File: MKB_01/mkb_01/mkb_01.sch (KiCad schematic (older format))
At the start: 360 parts, among them J1 USB_C_Receptacle_USB2.0, J2 SW_Push, K1 SW_Push, M1 SW_Push, P1 SW_Push, Q1 SW_Push, Q2 BSP318, Q3 BSP318, T1 SW_Push, U1 LD1117S33TR_SOT223, U2 STM32F070CBTx, U3 SW_Push, X1 SW_Push, Y1 SW_Push, Y2 Crystal

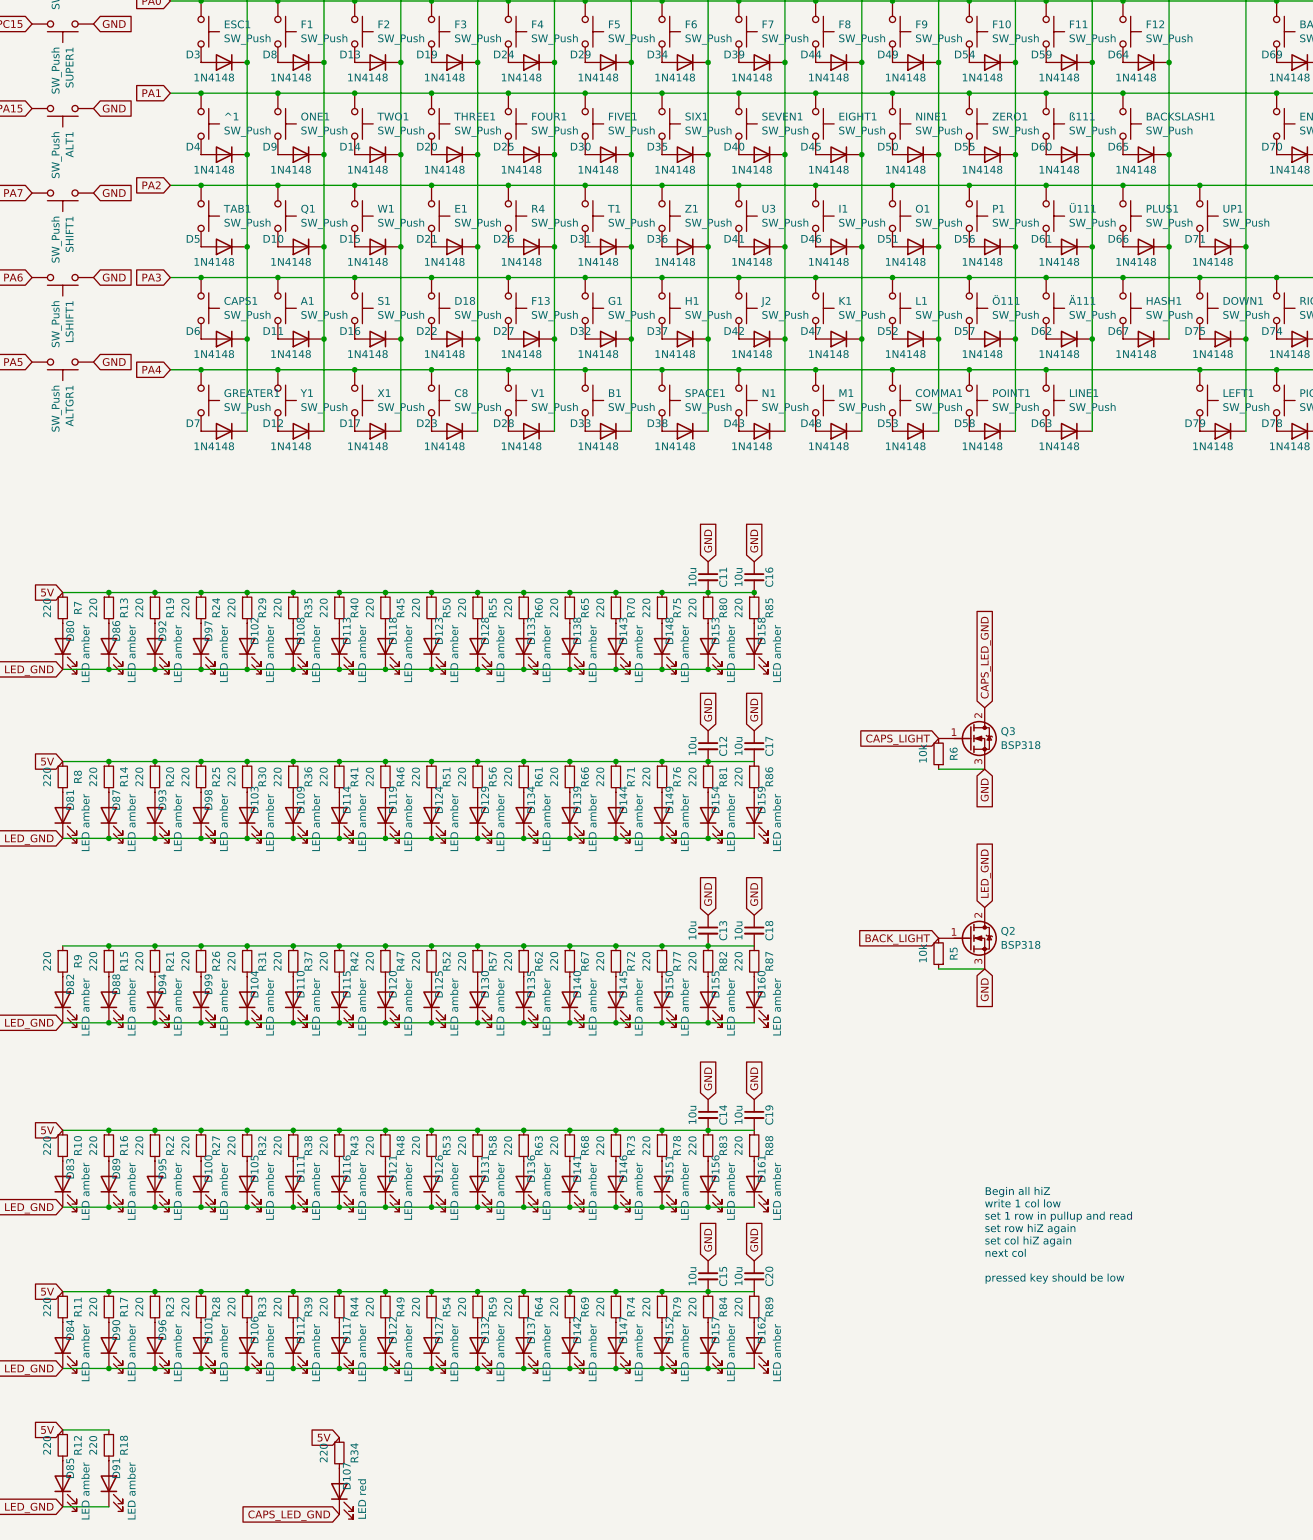
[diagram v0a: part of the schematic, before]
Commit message: added FN key fixed layout
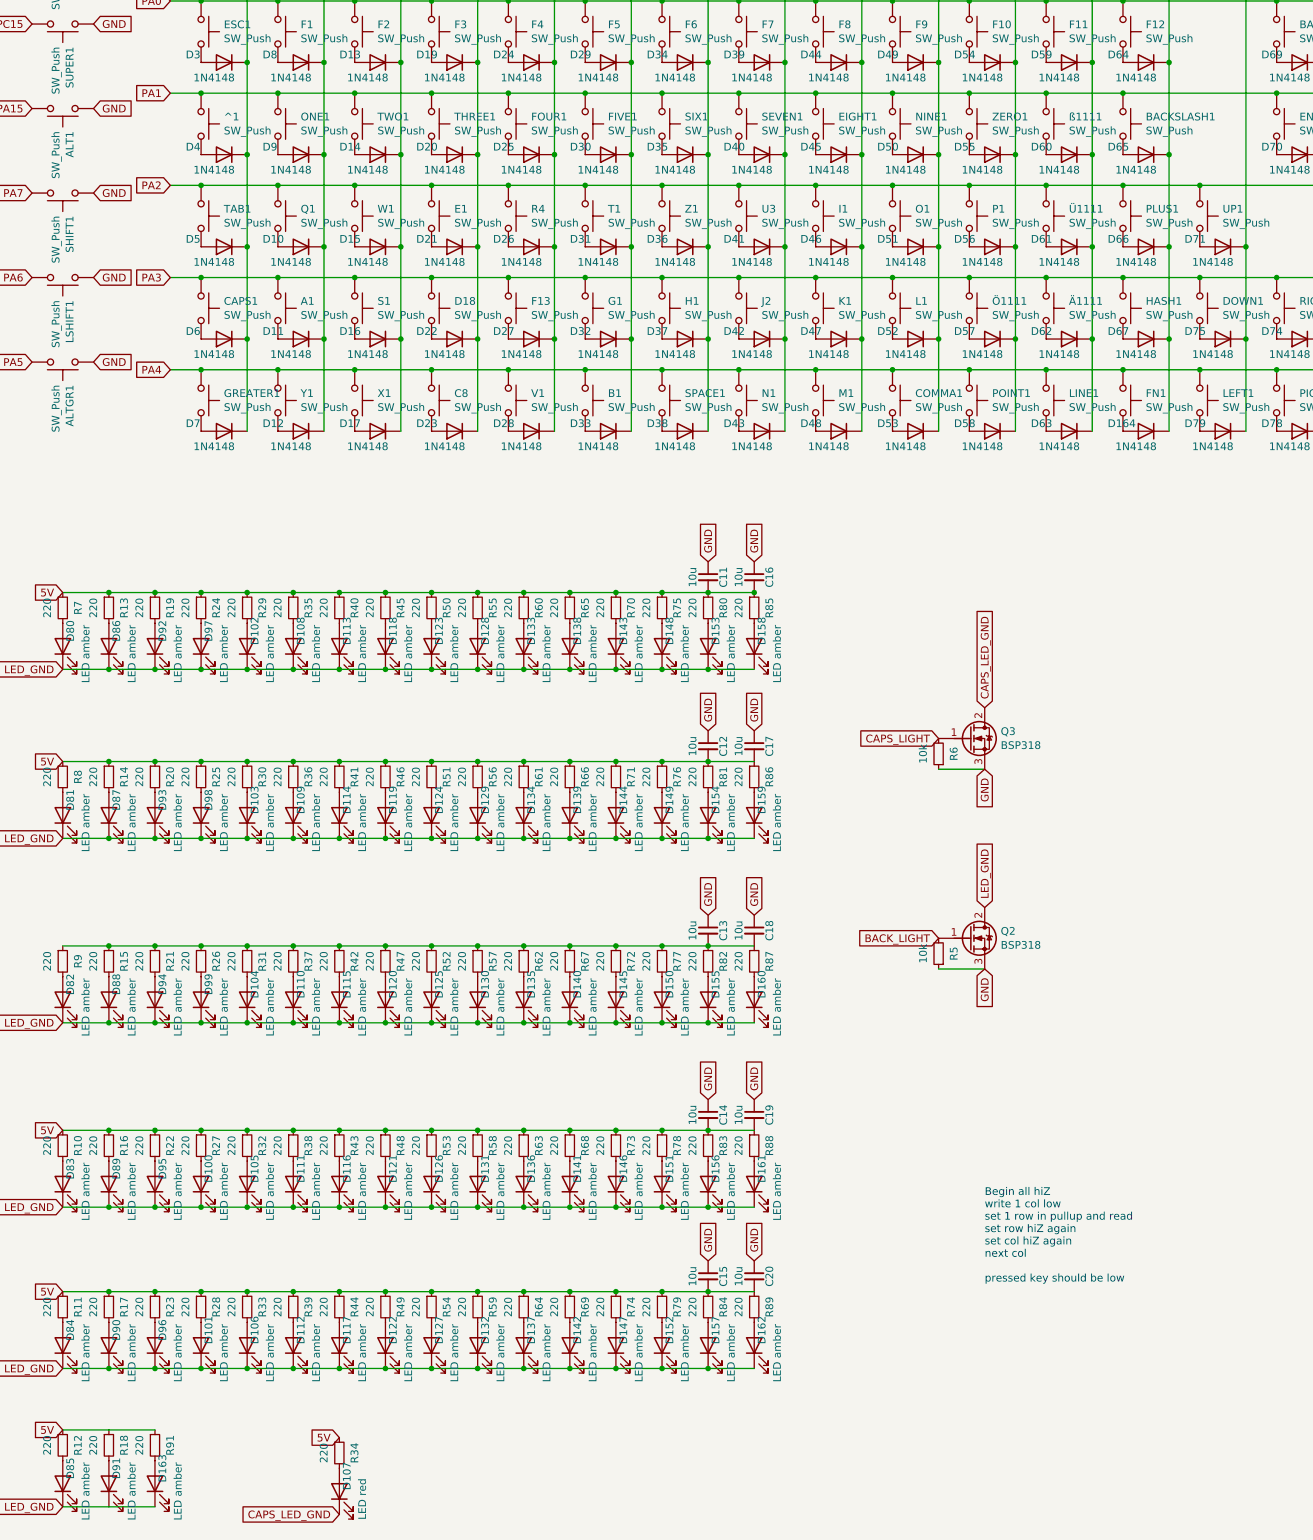
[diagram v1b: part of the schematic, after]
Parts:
- added D163: LED amber, LED_SMD:LED_0402_1005Metric_Pad0.77x0.64mm_HandSolder, symbol Device:LED
- added D164: 1N4148, Diode_SMD:D_0603_1608Metric_Pad1.05x0.95mm_HandSolder, symbol Diode:1N4148
- added FN1: SW_Push, Button_Switch_Keyboard:SW_Cherry_MX_1.00u_PCB, symbol Switch:SW_Push
- added R91: 220, Resistor_SMD:R_0603_1608Metric_Pad0.98x0.95mm_HandSolder, symbol Device:R_Small
- LSHIFT1, PICDOWN1, SUPER1: footprint Button_Switch_Keyboard:SW_Cherry_MX_1.25u_PCB -> Button_Switch_Keyboard:SW_Cherry_MX_1.00u_PCB
- SHIFT1: footprint Button_Switch_Keyboard:SW_Cherry_MX_1.25u_PCB -> Button_Switch_Keyboard:SW_Cherry_MX_2.00u_PCB
- renumbered Ä111 to Ä1111, Ö111 to Ö1111, Ü111 to Ü1111, ß111 to ß1111
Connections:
- net 5V: now also R91.1
- net LED_GND: now also D163.1 (K)
- net PA4: now also FN1.1
- net PB12: now also D164.1 (K)
- new net: D164.2 (A), FN1.2
- new net: D163.2 (A), R91.2
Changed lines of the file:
@@
 $EndComp
 $Comp
-L Switch:SW_Push ß111
+L Switch:SW_Push ß1111
 U 1 1 604A27F2
 P 13250 2000
-F 0 "ß111" V 13204 2148 50  0000 L CNN
+F 0 "ß1111" V 13204 2148 50  0000 L CNN
 F 1 "SW_Push" V 13295 2148 50  0000 L CNN
 F 2 "Button_Switch_Keyboard:SW_Cherry_MX_1.00u_PCB" H 13250 2200 50  0001 C CNN
@@
 $EndComp
 $Comp
-L Switch:SW_Push Ü111
+L Switch:SW_Push Ü1111
 U 1 1 604B7861
 P 13250 2600
-F 0 "Ü111" V 13204 2748 50  0000 L CNN
+F 0 "Ü1111" V 13204 2748 50  0000 L CNN
 F 1 "SW_Push" V 13295 2748 50  0000 L CNN
 F 2 "Button_Switch_Keyboard:SW_Cherry_MX_1.00u_PCB" H 13250 2800 50  0001 C CNN
@@
 F 0 "PICDOWN1" V 14704 3948 50  0000 L CNN
 F 1 "SW_Push" V 14795 3948 50  0000 L CNN
-F 2 "Button_Switch_Keyboard:SW_Cherry_MX_1.25u_PCB" H 14750 4000 50  0001 C CNN
+F 2 "Button_Switch_Keyboard:SW_Cherry_MX_1.00u_PCB" H 14750 4000 50  0001 C CNN
 F 3 "~" H 14750 4000 50  0001 C CNN
 	1    14750 3800
@@
 $EndComp
 $Comp
-L Switch:SW_Push Ö111
+L Switch:SW_Push Ö1111
 U 1 1 604C336A
 P 12750 3200
-F 0 "Ö111" V 12704 3348 50  0000 L CNN
+F 0 "Ö1111" V 12704 3348 50  0000 L CNN
 F 1 "SW_Push" V 12795 3348 50  0000 L CNN
 F 2 "Button_Switch_Keyboard:SW_Cherry_MX_1.00u_PCB" H 12750 3400 50  0001 C CNN
@@
 $EndComp
 $Comp
-L Switch:SW_Push Ä111
+L Switch:SW_Push Ä1111
 U 1 1 604C3376
 P 13250 3200
-F 0 "Ä111" V 13204 3348 50  0000 L CNN
+F 0 "Ä1111" V 13204 3348 50  0000 L CNN
 F 1 "SW_Push" V 13295 3348 50  0000 L CNN
 F 2 "Button_Switch_Keyboard:SW_Cherry_MX_1.00u_PCB" H 13250 3400 50  0001 C CNN
@@
 F 0 "SUPER1" V 6804 1498 50  0000 L CNN
 F 1 "SW_Push" V 6895 1498 50  0000 L CNN
-F 2 "Button_Switch_Keyboard:SW_Cherry_MX_1.25u_PCB" H 6850 1550 50  0001 C CNN
+F 2 "Button_Switch_Keyboard:SW_Cherry_MX_1.00u_PCB" H 6850 1550 50  0001 C CNN
 F 3 "~" H 6850 1550 50  0001 C CNN
 	1    6850 1350
@@
 F 0 "SHIFT1" V 6804 2598 50  0000 L CNN
 F 1 "SW_Push" V 6895 2598 50  0000 L CNN
-F 2 "Button_Switch_Keyboard:SW_Cherry_MX_1.25u_PCB" H 6850 2650 50  0001 C CNN
+F 2 "Button_Switch_Keyboard:SW_Cherry_MX_2.00u_PCB" H 6850 2650 50  0001 C CNN
 F 3 "~" H 6850 2650 50  0001 C CNN
 	1    6850 2450
@@
 F 0 "LSHIFT1" V 6804 3148 50  0000 L CNN
 F 1 "SW_Push" V 6895 3148 50  0000 L CNN
-F 2 "Button_Switch_Keyboard:SW_Cherry_MX_1.25u_PCB" H 6850 3200 50  0001 C CNN
+F 2 "Button_Switch_Keyboard:SW_Cherry_MX_1.00u_PCB" H 6850 3200 50  0001 C CNN
 F 3 "~" H 6850 3200 50  0001 C CNN
 	1    6850 3000
@@
 	14550 1100 14550 2800
 Wire Wire Line
-	13250 3600 14250 3600
+	13250 3600 13750 3600
 Connection ~ 13250 3600
 Connection ~ 14250 3600
@@
 	15550 3400 15550 4000
 Connection ~ 15550 3400
+$Comp
+L Switch:SW_Push FN1
+U 1 1 604CEAFC
+P 13750 3800
+F 0 "FN1" V 13704 3948 50  0000 L CNN
+F 1 "SW_Push" V 13795 3948 50  0000 L CNN
+F 2 "Button_Switch_Keyboard:SW_Cherry_MX_1.00u_PCB" H 13750 4000 50  0001 C CNN
+F 3 "~" H 13750 4000 50  0001 C CNN
+	1    13750 3800
+	0    1    1    0
+$EndComp
+$Comp
+L Diode:1N4148 D164
+U 1 1 604CEB02
+P 13900 4000
+F 0 "D164" H 14150 3950 50  0000 R CNN
+F 1 "1N4148" H 14100 4100 50  0000 R CNN
+F 2 "Diode_SMD:D_0603_1608Metric_Pad1.05x0.95mm_HandSolder" H 13900 3825 50  0001 C CNN
+F 3 "https://assets.nexperia.com/documents/data-sheet/1N4148_1N4448.pdf" H 13900 4000 50  0001 C CNN
+	1    13900 4000
+	-1   0    0    1
+$EndComp
+Connection ~ 13750 3600
+Wire Wire Line
+	13750 3600 14250 3600
+Wire Wire Line
+	14050 3400 14050 4000
+Connection ~ 14050 3400
+$Comp
+L Device:LED D163
+U 1 1 6056B7A9
+P 7450 10850
+F 0 "D163" H 7550 10800 50  0000 C CNN
+F 1 "LED amber" H 7400 10700 50  0000 C CNN
+F 2 "LED_SMD:LED_0402_1005Metric_Pad0.77x0.64mm_HandSolder" H 7450 10850 50  0001 C CNN
+F 3 "https://www.farnell.com/datasheets/2344828.pdf" H 7450 10850 50  0001 C CNN
+F 4 "https://de.farnell.com/broadcom-limited/hsma-c280/led-gelb-90mcd-592nm-0402/dp/2494320RL" H 7450 10850 50  0001 C CNN "URL"
+	1    7450 10850
+	0    -1   -1   0
+$EndComp
+$Comp
+L Device:R_Small R91
+U 1 1 6056B7B0
+P 7450 10600
+F 0 "R91" V 7550 10600 50  0000 C CNN
+F 1 "220" V 7350 10600 50  0000 C CNN
+F 2 "Resistor_SMD:R_0603_1608Metric_Pad0.98x0.95mm_HandSolder" H 7450 10600 50  0001 C CNN
+F 3 "~" H 7450 10600 50  0001 C CNN
+F 4 "https://de.farnell.com/walsin/wr06x221-jtl/dickschichtwiderstand-220r-5-0/dp/2670694" V 7450 10600 50  0001 C CNN "URL"
+	1    7450 10600
+	1    0    0    -1
+$EndComp
+Wire Wire Line
+	7150 10500 7450 10500
+Wire Wire Line
+	7150 11000 7450 11000
 $EndSCHEMATC

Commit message: changed quartz, finished placing and layers, some routing done
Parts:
- added H2, H3, H4, H5, H6, H7, H8, H9: MountingHole, MountingHole:MountingHole_3.2mm_M3_DIN965_Pad_TopBottom, symbol Mechanical:MountingHole
- Y2: footprint Crystal:Crystal_SMD_SeikoEpson_MA505-2Pin_12.7x5.1mm_HandSoldering -> Crystal:Crystal_SMD_Abracon_ABM3-2Pin_5.0x3.2mm_HandSoldering; URL https://de.farnell.com/iqd-frequency-products/lfxtal020423/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 -> https://de.farnell.com/abracon/abm3-8-000mhz-d2y-t/quarz-8m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
- renumbered LSHIFT1 to RSHIFT1, Ä1111 to Ä11111, Ö1111 to Ö11111, Ü1111 to Ü11111, ß1111 to ß11111
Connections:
- net 5V: now also C13.2, C18.2, R15.1, R21.1, R26.1, R31.1, R37.1, R42.1, R47.1, R52.1, R57.1, R62.1, R67.1, R72.1, R77.1, R82.1, R87.1, R9.1
- net PA0: now also POS1.1; no longer BACKSPACE1.1
- net PA1: now also BACKSPACE1.1, END1.1; no longer ENTER1.1
- net PA2: now also ENTER1.1, PICUP1.1; no longer POS1.1
- net PA3: now also PICDOWN1.1; no longer END1.1, RIGHT1.1
- net PA4: now also RIGHT1.1; no longer PICDOWN1.1, PICUP1.1
- net PB11: now also D164.1 (K); no longer D63.1 (K)
- net PB12: now also D63.1 (K); no longer D164.1 (K)
- net PB13: now also D69.1 (K), D70.1 (K)
- net PB14: now also D73.1 (K), D76.1 (K), D77.1 (K); no longer D69.1 (K), D70.1 (K)
- net PB15: no longer D73.1 (K), D76.1 (K), D77.1 (K)
- net PB5: now also D38.1 (K); no longer D33.1 (K)
- net PB6: now also D33.1 (K); no longer D38.1 (K)
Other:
- moved on the sheet: A1, ALT1, ALTGR1, B1, BACKSLASH1, BACKSPACE1, C11, C12, C13, C14, C15, C16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

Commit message: added ferrit beads and optimized pcb a bit
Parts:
- added FB1, FB2, FB3, FB4, FB5: Ferrite_Bead_Small, Inductor_SMD:L_0603_1608Metric_Pad1.05x0.95mm_HandSolder, symbol Device:Ferrite_Bead_Small
- renumbered Ä11111 to Ä1111111, Ö11111 to Ö1111111, Ü11111 to Ü1111111, ß11111 to ß1111111
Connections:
- net 3V3: now also FB1.1, FB2.1, FB3.1, FB4.1, FB5.1; no longer C2.1, C3.1, C5.1, C6.1, C7.1, U2.1 (VDD), U2.24 (VDD), U2.36 (VDD), U2.48 (VDD), U2.9 (VDDA)
- new net: C2.1, FB1.2, U2.1 (VDD)
- new net: C7.1, FB4.2, U2.9 (VDDA)
- new net: C6.1, FB3.2, U2.48 (VDD)
- new net: C3.1, FB5.2, U2.24 (VDD)
- new net: C5.1, FB2.2, U2.36 (VDD)
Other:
- moved on the sheet: C10, C2, C3, C5, C6, C7, C9, H2, H3, H4, H5, H6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
